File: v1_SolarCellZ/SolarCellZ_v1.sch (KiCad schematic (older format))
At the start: 14 parts, among them IC1 symbols_TSL2561, J1 symbols_XF2M-1015-1A

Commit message: Added the first layer of the magnetorquer
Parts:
- removed BW1: BurnWire, SolarCellParts:Burn-Wire-Rotated, symbol SolarCellParts:BurnWire
- removed IC1: symbols_TSL2561, misc-circuits:TSL2561, symbol misc-circuits-cache:symbols_TSL2561
- removed J1: symbols_XF2M-1015-1A, misc-circuits:XF2M-1015-1A, symbol misc-circuits-cache:symbols_XF2M-1015-1A
- added C1: 0.1uF, Capacitor_SMD:C_0402_1005Metric, symbol SolarCellZ_v1-rescue:0.1UF-0603-25V-(+80_-20%)-misc-circuits-cache-misc-circuit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
- added IC1: TSL2561, misc-circuits:TSL2561, symbol SolarCellZ_v1-rescue:TSL2561-symbols-misc-circuits-rescue
- added J1: XF2M-1015-1A, misc-circuits:XF2M-1015-1A, symbol SolarCellZ_v1-rescue:XF2M-1015-1A-symbols-misc-circuits-rescue
- added JP1: Jumper, SolarCellParts:Burn-Wire-Rotated, symbol Device:Jumper
- added Q1: IRLML2803, Package_TO_SOT_SMD:SOT-23, symbol SolarCellZ_v1-rescue:IRLML2803TRPBF-mainboard-misc-circuits-rescue
- added R1, R2: 0, Resistor_SMD:R_0402_1005Metric, symbol SolarCellZ_v1-rescue:0OHM-0603-1_10W-5%-misc-circuits-cache-misc-circuits-rescue
- added R3: 10k, Resistor_SMD:R_0402_1005Metric, symbol SolarCellZ_v1-rescue:RESISTOR0603-mainboard-misc-circuits-rescue
- added R4: 4.7k, Resistor_SMD:R_0402_1005Metric, symbol SolarCellZ_v1-rescue:RESISTOR0603-mainboard-misc-circuits-rescue
- added R5: 100k, Resistor_SMD:R_0402_1005Metric, symbol SolarCellZ_v1-rescue:RESISTOR0603-mainboard-misc-circuits-rescue
- added U1: NDS8434, misc-circuits:NDS8434, symbol SolarCellZ_v1-rescue:NDS8434-symbols-misc-circuits-rescue
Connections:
- net labels added: +3V3, BATT_N, BATT_P, BURN1, COIL_N, COIL_P, GND, SCL1, SDA1, VBURN, VSolar
- wire segments 19 -> 64
- no-connect marks 0 -> 1
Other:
- note added: "Burn Wire Control (Antenna Depolyment)"
- note added: "Flat Flex Connector"
- moved on the sheet: D1, D2, D3, SC1, SC2, SC3, SC4, SC5, SC6, SC7, SC8

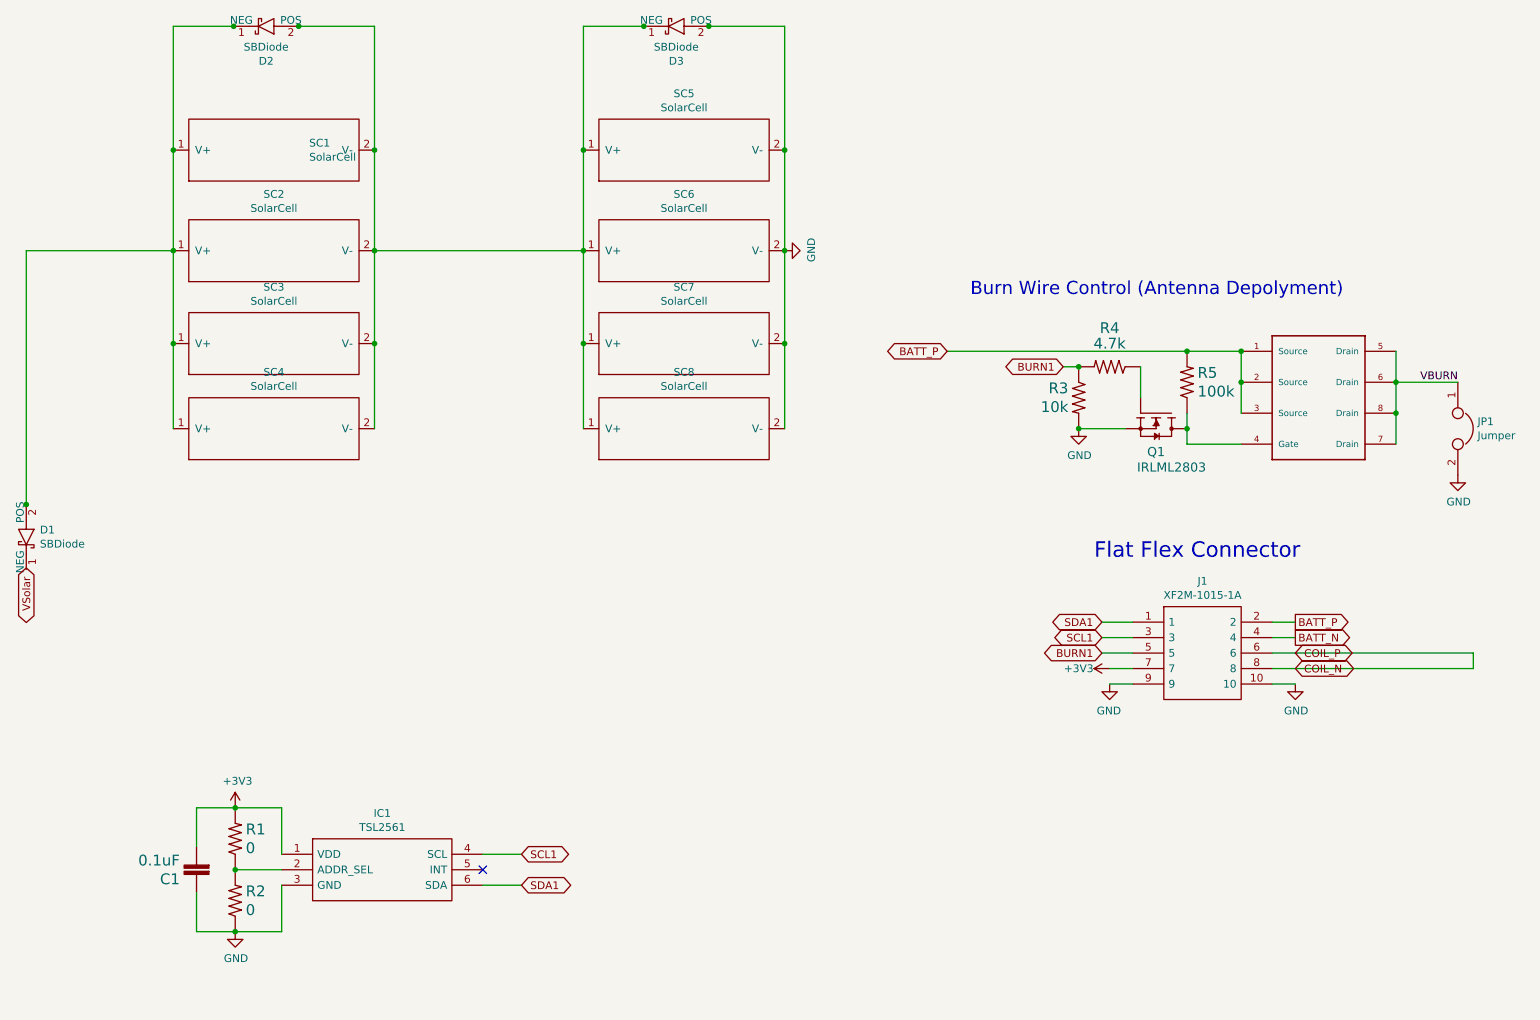
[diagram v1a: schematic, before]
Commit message: X and Z panels are ready
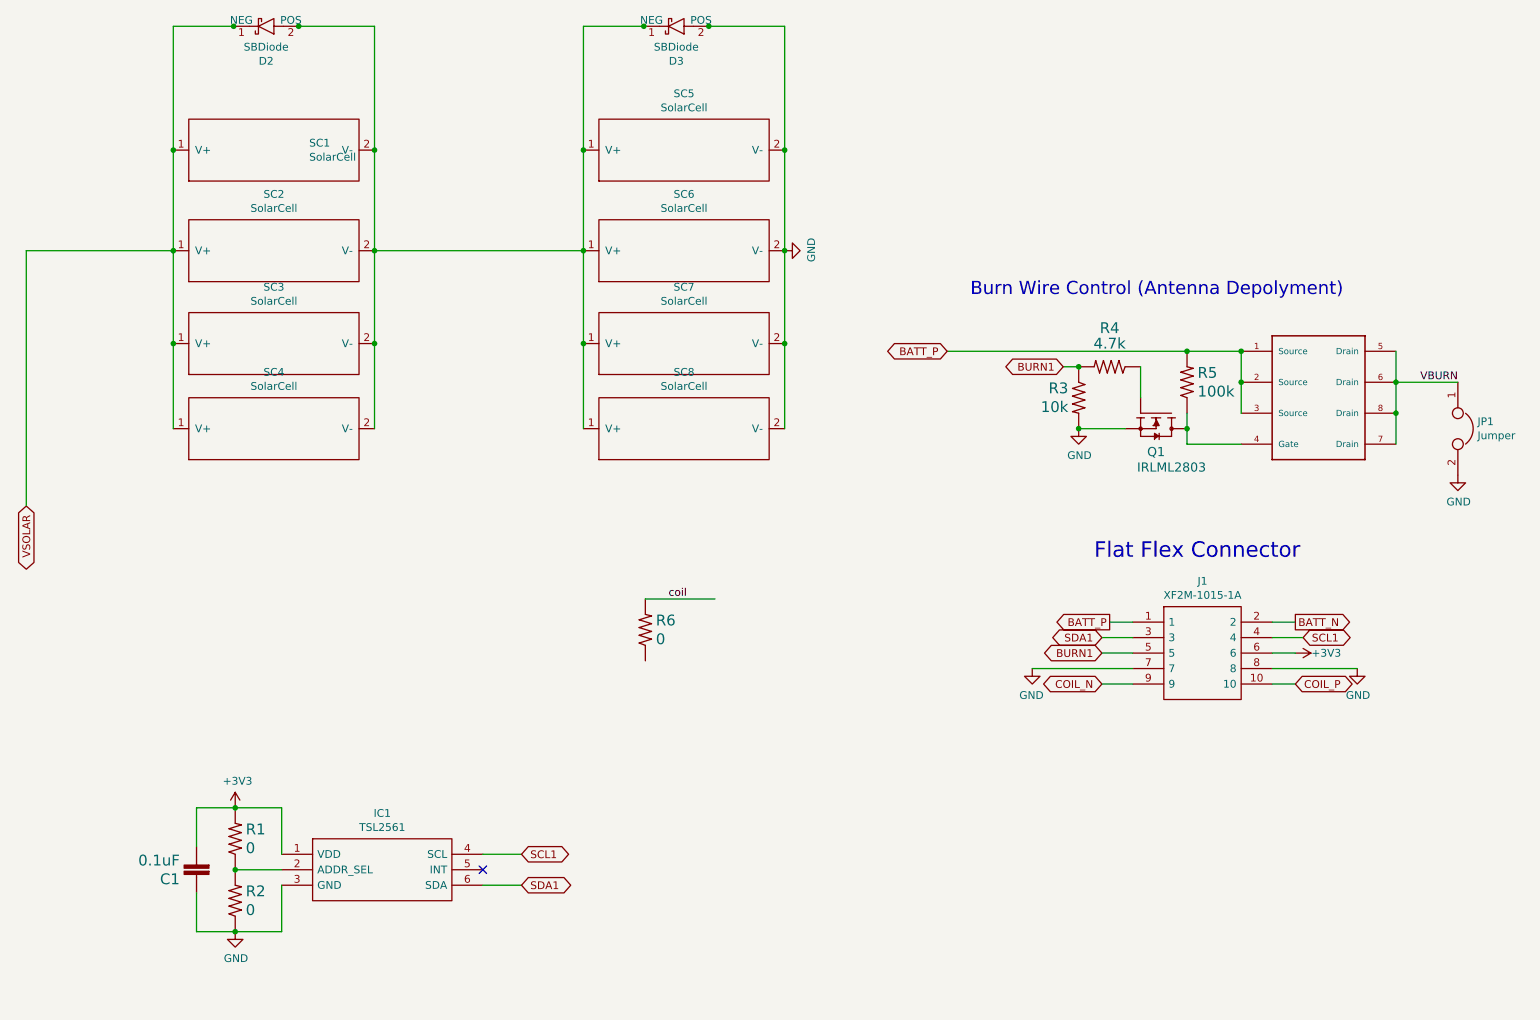
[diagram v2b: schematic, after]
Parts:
- removed D1: SBDiode, SolarCellParts:SB Diode, symbol SolarCellParts:SBDiode
- added R6: 0, Resistor_SMD:R_0402_1005Metric, symbol SolarCellZ_v1-rescue:0OHM-0603-1_10W-5%-misc-circuits-cache-misc-circuits-rescue
- U1: footprint misc-circuits:NDS8434 -> custom-footprints:NDS8434
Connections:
- net labels added: VSOLAR, coil
- net labels removed: VSolar
- wire segments 64 -> 63
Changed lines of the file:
@@
 EESchema Schematic File Version 4
 LIBS:SolarCellZ_v1-cache
-LIBS:misc-circuits-cache
 EELAYER 30 0
 EELAYER END
@@
 	-1   0    0    1
 $EndComp
-$Comp
-L SolarCellParts:SBDiode D1
-U 1 1 5DB1BFED
-P 900 4250
-F 0 "D1" V 804 4338 50  0000 L CNN
-F 1 "SBDiode" V 895 4338 50  0000 L CNN
-F 2 "SolarCellParts:SB Diode" H 780 4580 50  0001 C CNN
-F 3 "" H 840 4370 50  0001 C CNN
-	1    900  4250
-	0    1    1    0
-$EndComp
 Connection ~ 1850 2350
 Wire Wire Line
@@
 Wire Wire Line
 	1850 2350 900  2350
-Wire Wire Line
-	900  2350 900  3990
-Connection ~ 900  3990
-Wire Wire Line
-	900  3990 900  4000
 Wire Wire Line
 	3150 2350 4500 2350
@@
 F 0 "U1" H 9250 3300 50  0001 L BNN
 F 1 "NDS8434" H 9250 3300 50  0001 L BNN
-F 2 "misc-circuits:NDS8434" H 9250 3300 50  0001 L BNN
+F 2 "custom-footprints:NDS8434" H 9250 3300 50  0001 L BNN
 F 3 "" H 9250 3300 50  0001 L BNN
 F 4 "DMP2022LSS-13" H 9250 3300 50  0001 L BNN "Proto"
@@
 BATT_P
 Wire Wire Line
-	8950 4750 9100 4750
+	8050 4750 7900 4750
+Text GLabel 7900 4750 0    50   Output ~ 0
+BATT_P
 Text GLabel 9100 4750 2    50   Output ~ 0
-BATT_P
-Text GLabel 9100 4850 2    50   Output ~ 0
 BATT_N
 Wire Wire Line
-	9100 4850 8950 4850
+	9100 4750 8950 4750
 $Comp
 L power:GND #PWR07
 U 1 1 5DB779CC
-P 9100 5150
-F 0 "#PWR07" H 9100 4900 50  0001 C CNN
-F 1 "GND" H 9105 4977 50  0000 C CNN
-F 2 "" H 9100 5150 50  0001 C CNN
-F 3 "" H 9100 5150 50  0001 C CNN
-	1    9100 5150
-	1    0    0    -1
-$EndComp
-Wire Wire Line
-	8950 5150 9100 5150
+P 9500 5050
+F 0 "#PWR07" H 9500 4800 50  0001 C CNN
+F 1 "GND" H 9505 4877 50  0000 C CNN
+F 2 "" H 9500 5050 50  0001 C CNN
+F 3 "" H 9500 5050 50  0001 C CNN
+	1    9500 5050
+	1    0    0    -1
+$EndComp
 $Comp
 L power:+3V3 #PWR05
 U 1 1 5DB87DA5
-P 7900 5050
-F 0 "#PWR05" H 7900 4900 50  0001 C CNN
-F 1 "+3V3" V 7900 5250 50  0000 C CNN
-F 2 "" H 7900 5050 50  0001 C CNN
-F 3 "" H 7900 5050 50  0001 C CNN
-	1    7900 5050
-	0    -1   -1   0
-$EndComp
-Wire Wire Line
-	8050 5050 7900 5050
+P 9100 4950
+F 0 "#PWR05" H 9100 4800 50  0001 C CNN
+F 1 "+3V3" V 9100 5150 50  0000 C CNN
+F 2 "" H 9100 4950 50  0001 C CNN
+F 3 "" H 9100 4950 50  0001 C CNN
+	1    9100 4950
+	0    1    1    0
+$EndComp
+Wire Wire Line
+	8950 4950 9100 4950
 $Comp
 L SolarCellZ_v1-rescue:TSL2561-symbols-misc-circuits-rescue IC1
@@
 	2000 6750 2250 6750
 NoConn ~ 3850 6350
+Text GLabel 9150 4850 2    50   BiDi ~ 0
+SCL1
+Wire Wire Line
+	9150 4850 8950 4850
 Text GLabel 7850 4850 0    50   BiDi ~ 0
-SCL1
+SDA1
 Wire Wire Line
 	7850 4850 8050 4850
-Text GLabel 7850 4750 0    50   BiDi ~ 0
-SDA1
-Wire Wire Line
-	7850 4750 8050 4750
 Text GLabel 7850 4950 0    50   BiDi ~ 0
 BURN1
 Wire Wire Line
 	7850 4950 8050 4950
-Text GLabel 9100 4950 2    50   BiDi ~ 0
+Text GLabel 9100 5150 2    50   BiDi ~ 0
 COIL_P
-Text GLabel 9100 5050 2    50   BiDi ~ 0
+Text GLabel 7850 5150 0    50   BiDi ~ 0
 COIL_N
 $Comp
 L power:GND #PWR06
 U 1 1 5DB7ADC7
-P 7900 5150
-F 0 "#PWR06" H 7900 4900 50  0001 C CNN
-F 1 "GND" H 7905 4977 50  0000 C CNN
-F 2 "" H 7900 5150 50  0001 C CNN
-F 3 "" H 7900 5150 50  0001 C CNN
-	1    7900 5150
+P 7400 5050
+F 0 "#PWR06" H 7400 4800 50  0001 C CNN
+F 1 "GND" H 7405 4877 50  0000 C CNN
+F 2 "" H 7400 5050 50  0001 C CNN
+F 3 "" H 7400 5050 50  0001 C CNN
+	1    7400 5050
 	-1   0    0    -1
 $EndComp
-Wire Wire Line
-	8050 5150 7900 5150
 Wire Wire Line
 	4100 6450 3850 6450
@@
 Text Notes 7800 4350 0    100  ~ 0
 Flat Flex Connector
-Text GLabel 900  4400 3    50   BiDi ~ 0
-VSolar
 $Comp
 L power:GND #PWR03
@@
 $EndComp
 Wire Wire Line
-	10250 4950 10250 5050
-Wire Wire Line
-	8950 4950 10250 4950
-Wire Wire Line
-	8950 5050 10250 5050
+	7850 5150 8050 5150
+Wire Wire Line
+	9100 5150 8950 5150
+Wire Wire Line
+	8950 5050 9500 5050
+Wire Wire Line
+	7400 5050 8050 5050
+Wire Wire Line
+	900  2350 900  4000
+Text GLabel 900  4000 3    50   BiDi ~ 0
+VSOLAR
+Wire Wire Line
+	4900 4600 5350 4600
+Text Label 5050 4600 0    50   ~ 0
+coil
+$Comp
+L SolarCellZ_v1-rescue:0OHM-0603-1_10W-5%-misc-circuits-cache-misc-circuits-rescue R6
+U 1 1 5DB6156D
+P 4900 4800
+F 0 "R6" V 4961 4732 70  0000 R CNN
+F 1 "0" V 4840 4732 70  0000 R CNN
+F 2 "Resistor_SMD:R_0402_1005Metric" H 4900 4800 50  0001 C CNN
+F 3 "" H 4900 4800 50  0001 C CNN
+	1    4900 4800
+	0    -1   -1   0
+$EndComp
 $EndSCHEMATC
